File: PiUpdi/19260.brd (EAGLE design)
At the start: 71.1 x 33 mm, 31 parts, among them J1 PPPC101LFBN, J3 PPPC101LFBN, J4 PPPC101LFBN, J5 40 PIN HDR, Q1 DMB, Q2 K38, Q3 K38, Q4 K84, U1 I50115H, U2 Z4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

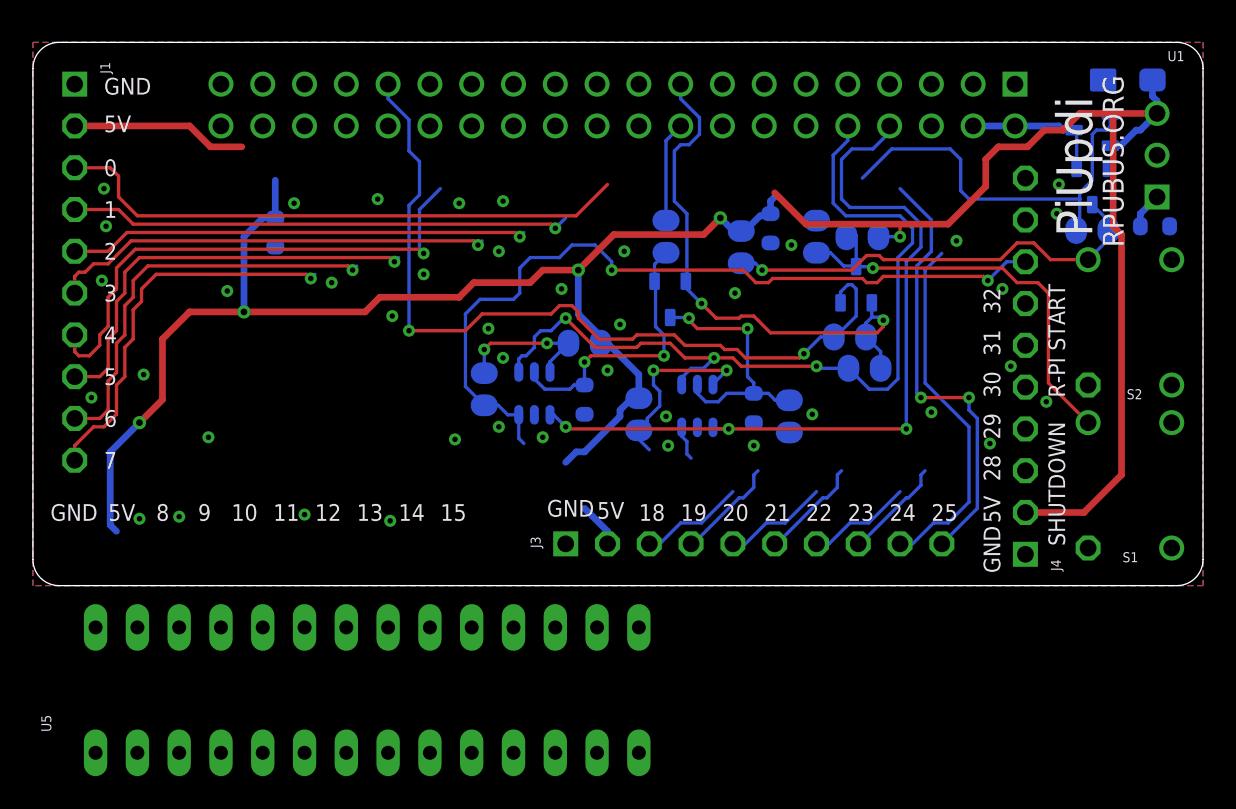
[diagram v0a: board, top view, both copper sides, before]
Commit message: PiUpdi: ^1 layout wip
serial crossover error fixed
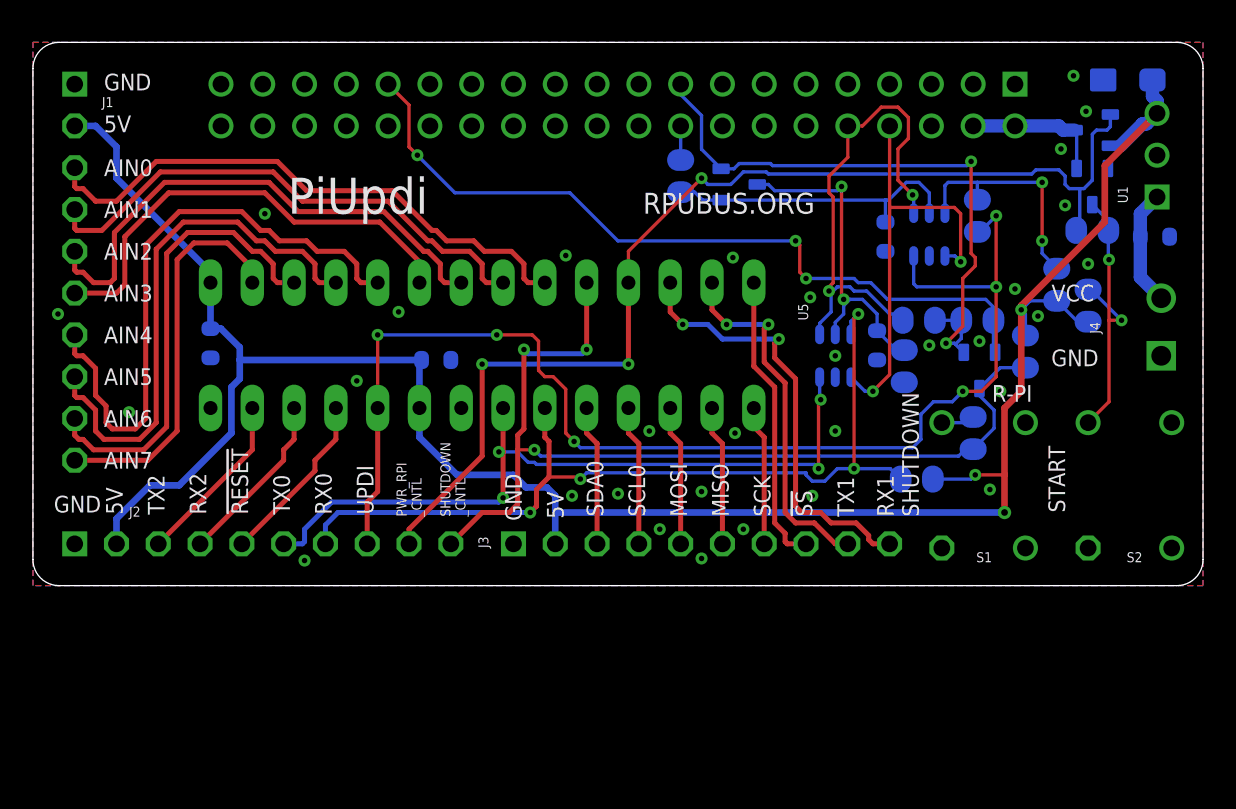
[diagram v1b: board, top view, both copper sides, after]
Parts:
- added J2: PPPC101LFBN, J-HDR2.54mm:F1X10
- J4: value PPPC101LFBN -> PST1,0/2-3,5; device J-HDR2.54mm:F1X10 -> J-HDR3.5mm:MCV2
- moved C5 34.7 mm to (10.8, 14.7)
- moved R10 31.8 mm to (57.4, 22.5)
- moved R9 28.9 mm to (62.2, 18.3), turned to 90 degrees
- moved U4 25.9 mm to (54.5, 21.3)
- moved U5 22.1 mm to (27.3, 14.6), turned to 180 degrees
- moved R2 21.4 mm to (64.1, 17.0), turned to 90 degrees
- moved C7 20.8 mm to (51.8, 21.2)
- moved R7 17.3 mm to (53.7, 6.48), turned to 0 degrees
- moved R3 15.3 mm to (57.1, 9.27), turned to 90 degrees
- moved J4 14.6 mm to (68.6, 14.0)
- moved C4 12.5 mm to (24.5, 13.7), turned to 180 degrees
- moved R4 12.1 mm to (60.3, 14.2), turned to 270 degrees
- moved S2 9.91 mm to (66.7, 6.10)
- moved Q3 9.12 mm to (57.5, 13.1), turned to 180 degrees
- moved U2 8.92 mm to (48.8, 14.0)
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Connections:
- removed net N$3: Q3.3(D), R3.2, R4.2, S1.2
- removed net VIN: C1.1, U1.1
- new net N$1: R3.2, S1.2
- new net VCC: C1.1, J4.2, U1.1
- net !RESET: now also J2.5; no longer J4.5
- net +5V: now also J2.2; no longer J4.2
- net 0V: now also J2.1
- net PWR_RPI_CNTL: now also J2.9; no longer J4.9
- net RX0: now also J2.7, R7.2, U2.6; no longer J4.7, U2.3
- net RX2: now also J2.4; no longer J4.4
- net SHUTDOWN_CNTL: now also J2.10, Q3.3(D), R4.2; no longer J4.10
- net TX0: now also J2.6, U2.3; no longer J4.6, R7.2, U2.6
- net TX2: now also J2.3; no longer J4.3
- net UPDI: now also J2.8; no longer J4.8
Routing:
- net SHUTDOWN_CNTL: track 0.00 -> 58.6 mm, vias 0 -> 3
- net RX0: track 2.11 -> 54.2 mm, vias 0 -> 4
- net PWR_RPI_CNTL: track 24.6 -> 67.6 mm, vias 0 -> 3
- net TX0: track 11.4 -> 46.1 mm, vias 2 -> 4
- net UPDI: track 49.1 -> 76.8 mm, vias 2 -> 6
- net N$3: track 26.5 -> 0.00 mm, vias 1 -> 0
- net +5V: track 158.6 -> 135.6 mm, vias 5 -> 3
- net TX_: track 47.7 -> 26.7 mm, vias 3 -> 2
- net RX_: track 50.4 -> 30.5 mm, vias 3 -> 2
- net !SS: track 6.28 -> 17.9 mm
- net TX2: track 0.00 -> 10.6 mm
- net RX2: track 0.00 -> 10.6 mm
- net !RESET: track 0.00 -> 10.6 mm
- net N$6: track 26.8 -> 17.8 mm, vias 1 -> 2
- net VCC: track 0.00 -> 7.10 mm
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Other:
- board text added: "!RESET"
- board text added: "!SS"
- board text added: "19260^1"
- board text added: "AIN0"
- board text added: "AIN1"
- board text added: "AIN2"
- board text added: "AIN3"
- board text added: "AIN4"
- board text added: "AIN5"
- board text added: "AIN6"
- board text added: "AIN7"
- board text added: "MISO"
- board text added: "MOSI"
- board text added: "PWR_RPI _CNTL"
- board text added: "R-PI"
- board text added: "RX0"
- board text added: "RX1"
- board text added: "RX2"
- board text added: "SCK"
- board text added: "SCL0"
- board text added: "SDA0"
- board text added: "SHUTDOWN _CNTL"
- board text added: "START"
- board text added: "TX0"
- board text added: "TX1"
- board text added: "TX2"
- board text added: "UPDI"
- board text added: "VCC"
- board text removed: "0"
- board text removed: "10"
- board text removed: "11"
- board text removed: "12"
- board text removed: "13"
- board text removed: "14"
- board text removed: "15"
- board text removed: "18"
- board text removed: "19"
- board text removed: "19260^0"
- board text removed: "2"
- board text removed: "20"
- board text removed: "21"
- board text removed: "22"
- board text removed: "23"
- board text removed: "24"
- board text removed: "25"
- board text removed: "28"
- board text removed: "29"
- board text removed: "3"
- board text removed: "30"
- board text removed: "31"
- board text removed: "32"
- board text removed: "4"
- board text removed: "5"
- board text removed: "6"
- board text removed: "7"
- board text removed: "8"
- board text removed: "9"
- board text removed: "R-PI START"

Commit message: PiUpdi: review
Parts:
- added R12: 3.01k, R-C:C0805(2012)
- R10: value 3.01k -> 1.82k
- R11: value 1.82k -> 3.01k
- R3: value 1k -> 100k
- R4: value 10k -> 1k
- R7: value 3.01k -> 182
- R8: value 10k -> 3.01k
- R9: value 3.01k -> 10k
- moved R7 23.3 mm to (39.4, 24.9), turned to 270 degrees
- moved R9 10.5 mm to (53.0, 13.3), turned to 270 degrees
- moved R6 8.89 mm to (30.5, 24.8), turned to 0 degrees
- moved R11 8.66 mm to (62.2, 18.3), turned to 90 degrees
- moved R10 7.28 mm to (53.8, 16.1), turned to 0 degrees
- moved R8 6.90 mm to (53.7, 6.48), turned to 0 degrees
- moved R3 5.88 mm to (60.3, 14.2), turned to 270 degrees
- moved R4 5.88 mm to (57.1, 9.27), turned to 90 degrees
- renumbered C7 to C6, U5 to U3
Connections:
- new net N$3: J5.31, R6.2
- net !UPDI_: now also R9.1; no longer R8.1
- net +3V3: now also R10.1; no longer R11.1
- net +5V: now also R11.1, R3.1, R8.1; no longer R4.1, R7.1, R9.1
- net 0V: now also R9.2; no longer R8.2
- net N$1: now also R4.2; no longer R3.2
- net N$2: now also R7.1; no longer R6.1
- net N$4: now also R11.2, R12.2; no longer R10.2, R9.2
- net RX0: now also R8.2; no longer R7.2
- net RX_: now also R10.2; no longer R11.2
- net SHUTDOWN: now also R6.1; no longer J5.31
- net SHUTDOWN_CNTL: now also R3.2, R4.1; no longer R3.1, R4.2
- net UPDI: now also R12.1; no longer R10.1
- net UPDI_: now also R7.2; no longer R6.2
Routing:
- net SHUTDOWN: track 47.6 -> 33.9 mm, vias 3 -> 2
- net N$3: track 0.00 -> 12.0 mm, vias 0 -> 1
